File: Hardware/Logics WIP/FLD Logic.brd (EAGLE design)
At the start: 60.6 x 33 mm, 82 parts

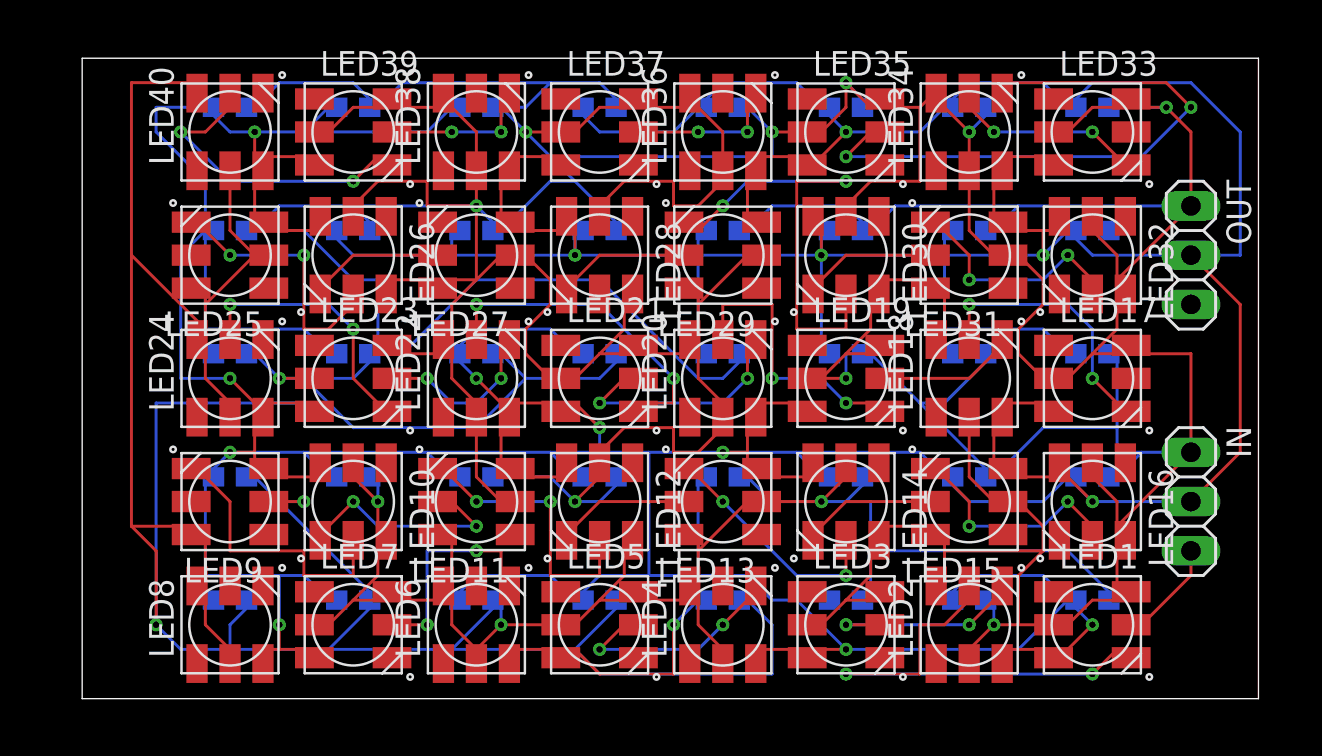
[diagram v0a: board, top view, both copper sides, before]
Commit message: 
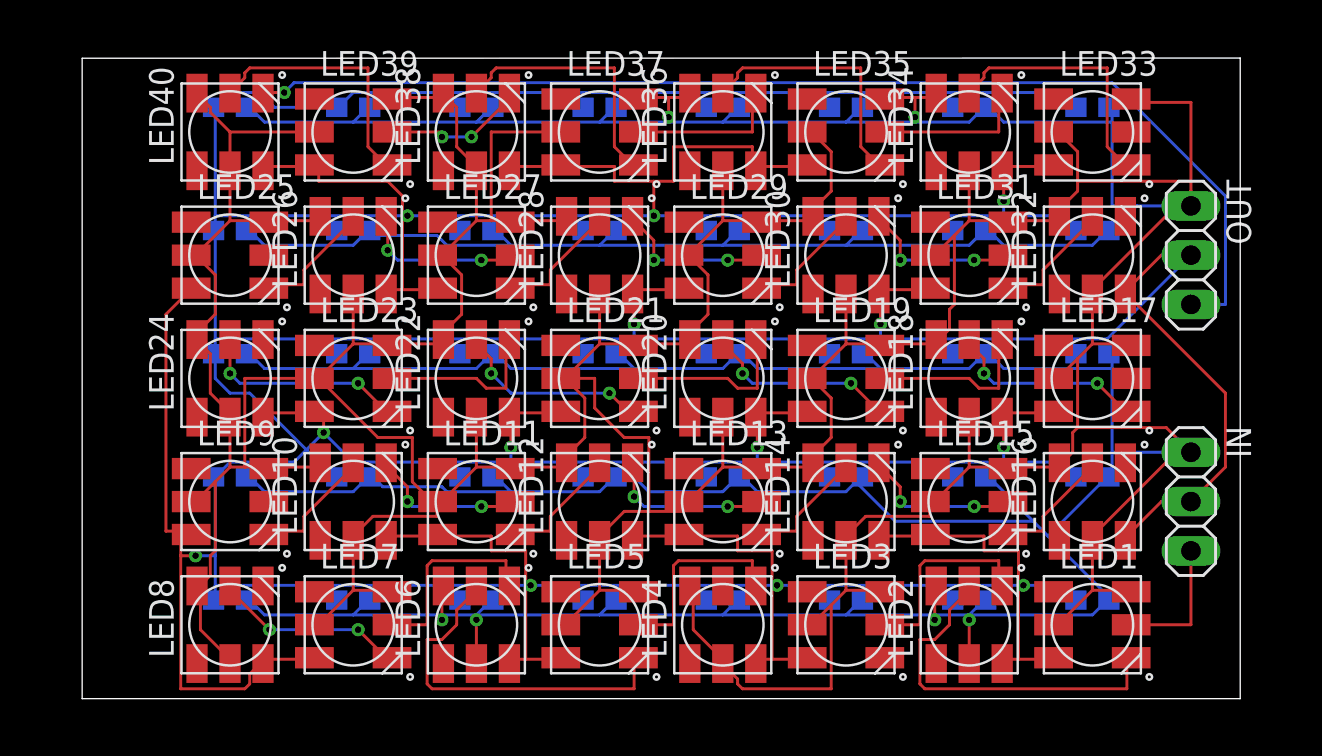
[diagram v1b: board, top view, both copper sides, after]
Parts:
- turned LED10 to 90 degrees
- turned LED11 to 0 degrees
- turned LED12 to 90 degrees
- turned LED13 to 0 degrees
- turned LED14 to 90 degrees
- turned LED15 to 0 degrees
- turned LED16 to 90 degrees
- turned LED25 to 0 degrees
- turned LED26 to 90 degrees
- turned LED27 to 0 degrees
- turned LED28 to 90 degrees
- turned LED29 to 0 degrees
- turned LED30 to 90 degrees
- turned LED31 to 0 degrees
- turned LED32 to 90 degrees
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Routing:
- net +5V: track 746.6 -> 637.9 mm, vias 15 -> 6
- net DOUT: track 0.00 -> 59.6 mm, vias 0 -> 1
- net N$33: track 32.7 -> 7.94 mm, vias 2 -> 0
- net N$2: track 0.00 -> 19.1 mm
- net GND: track 496.5 -> 478.6 mm, vias 15 -> 13
- net N$27: track 24.0 -> 6.53 mm, vias 2 -> 0
- net N$35: track 0.00 -> 13.6 mm
- net N$36: track 0.00 -> 13.6 mm
- net N$4: track 0.00 -> 10.1 mm, vias 0 -> 2
- net N$13: track 14.6 -> 6.53 mm, vias 2 -> 0
- net N$7: track 14.6 -> 6.53 mm
- net N$24: track 13.9 -> 6.53 mm, vias 2 -> 0
- net N$28: track 0.00 -> 6.53 mm
- net N$11: track 25.5 -> 19.1 mm, vias 2 -> 0
- net N$19: track 16.8 -> 10.4 mm
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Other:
- board size 60.6 x 33 mm -> 59.7 x 33 mm

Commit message: 
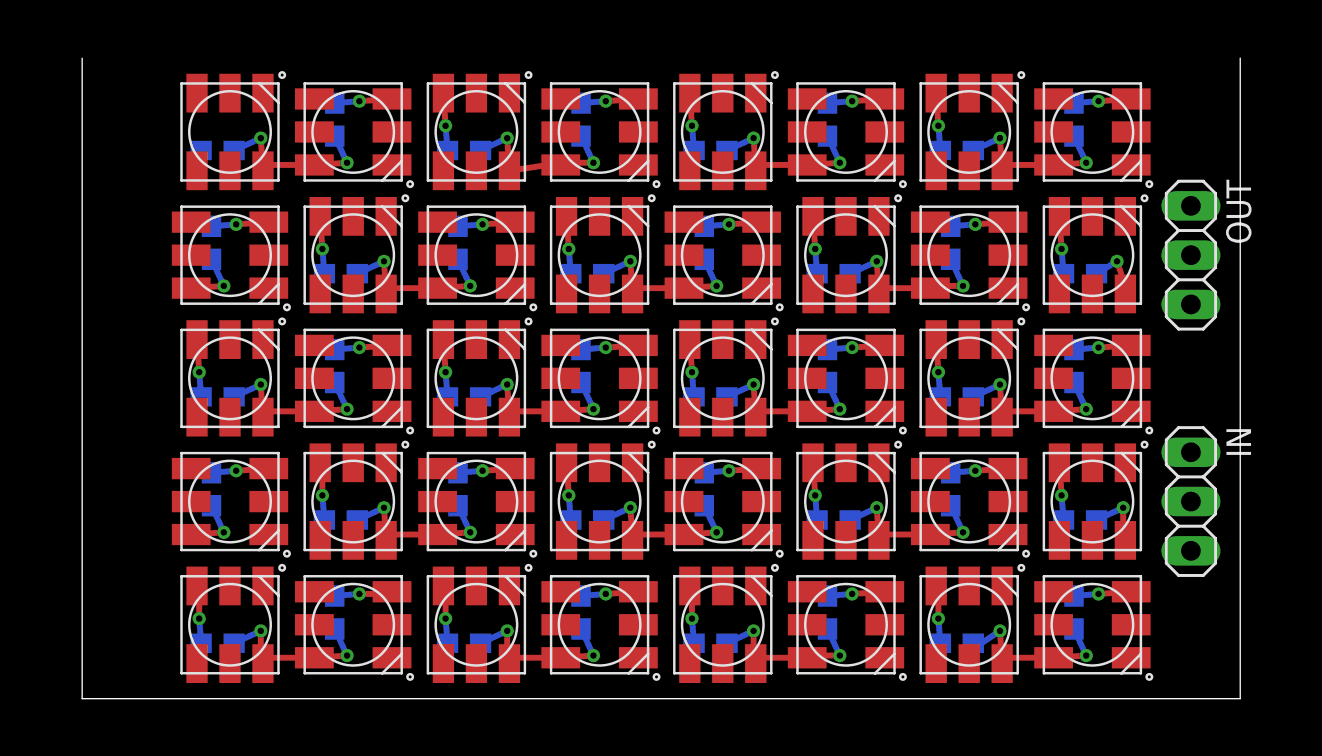
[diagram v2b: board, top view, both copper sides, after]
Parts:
- moved C20 2.31 mm to (32.4, 15.6), turned to 180 degrees
- moved C22 2.31 mm to (19.7, 15.6), turned to 180 degrees
- moved C24 2.31 mm to (6.99, 15.6), turned to 180 degrees
- moved C18 2.31 mm to (45.1, 15.6), turned to 180 degrees
- moved C36 2.31 mm to (32.4, 28.3), turned to 180 degrees
- moved C4 2.31 mm to (32.4, 2.86)
- moved C12 2.31 mm to (26.0, 9.21), turned to 180 degrees
- moved C28 2.31 mm to (26.0, 21.9), turned to 180 degrees
- moved C38 2.31 mm to (19.7, 28.3), turned to 180 degrees
- moved C6 2.31 mm to (19.7, 2.86), turned to 180 degrees
- moved C10 2.31 mm to (13.3, 9.21), turned to 180 degrees
- moved C26 2.31 mm to (13.3, 21.9), turned to 180 degrees
- moved C40 2.31 mm to (6.99, 28.3), turned to 180 degrees
- moved C8 2.31 mm to (6.99, 2.86), turned to 180 degrees
- moved C14 2.31 mm to (38.7, 9.21), turned to 180 degrees
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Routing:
- net +5V: track 637.9 -> 109.1 mm, vias 6 -> 38
- net GND: track 478.6 -> 174.8 mm, vias 13 -> 41
- net DOUT: track 59.6 -> 0.00 mm, vias 1 -> 0
- net N$2: track 19.1 -> 0.00 mm
- net N$11: track 19.1 -> 0.00 mm
- net N$37: track 13.6 -> 0.00 mm
- net N$35: track 13.6 -> 0.00 mm
- net N$32: track 13.6 -> 0.00 mm
- net N$36: track 13.6 -> 0.00 mm
- net N$21: track 11.0 -> 0.00 mm, vias 2 -> 0
- net N$6: track 10.5 -> 0.00 mm, vias 2 -> 0
- net N$12: track 10.5 -> 0.00 mm
- net N$5: track 10.5 -> 0.00 mm
- net N$1: track 10.5 -> 0.00 mm
- net N$19: track 10.4 -> 0.00 mm, vias 2 -> 0
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
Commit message: 
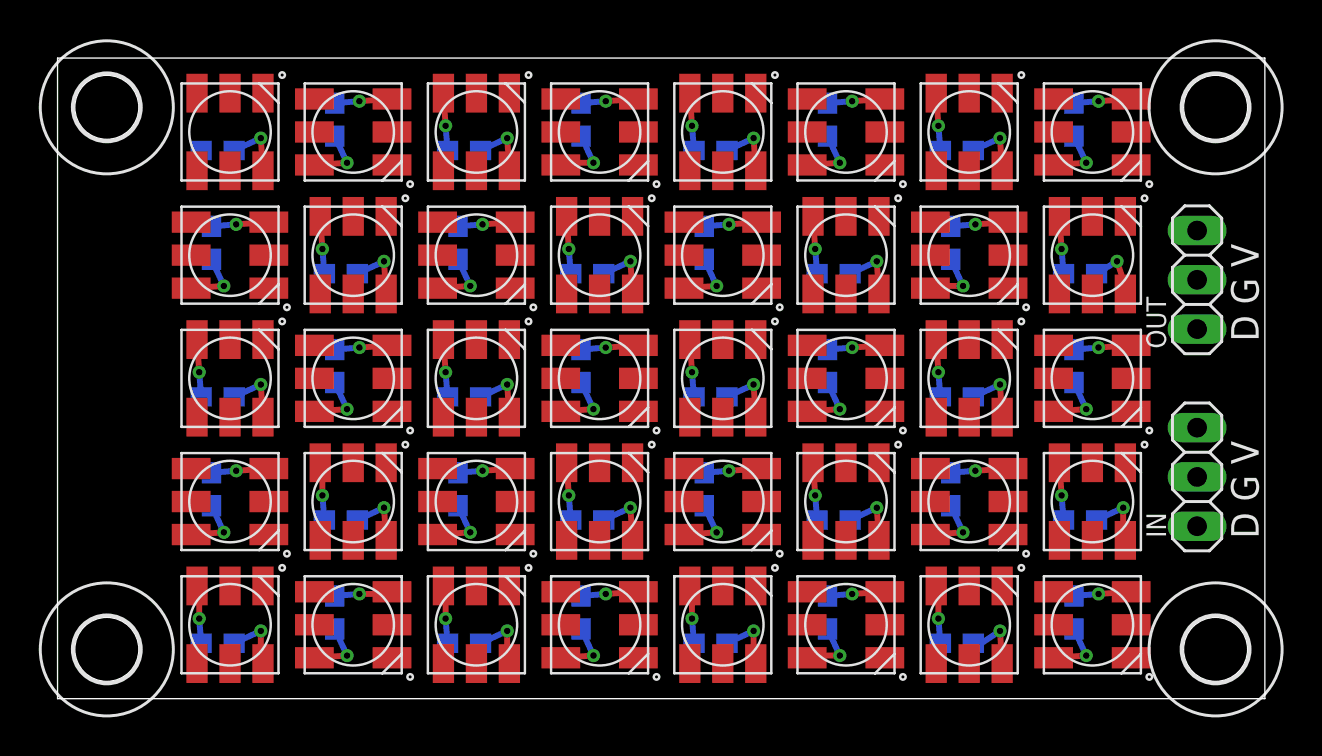
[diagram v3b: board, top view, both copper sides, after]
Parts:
- added H1, H2, H3, H4: MOUNT-HOLE3.3, holes:3,3
- moved IN 1.31 mm to (57.5, 11.4)
- moved OUT 1.31 mm to (57.5, 21.6)
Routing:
- net GND: track 174.8 -> 128.2 mm
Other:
- board size 59.7 x 33 mm -> 62.2 x 33 mm
- board text added: "D G V"

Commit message: 
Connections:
- net +5V: now also IN.2, OUT.2; no longer IN.1, OUT.1
- net GND: now also IN.1, OUT.1; no longer IN.2, OUT.2
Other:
- board text added: "D + G"
- board text removed: "D G V"
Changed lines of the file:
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@@
 <setting verticaltext="up"/>
 </settings>
-<grid distance="0.0125" unitdist="inch" unit="inch" style="lines" multiple="1" display="yes" altdistance="0.025" altunitdist="inch" altunit="inch"/>
+<grid distance="0.05" unitdist="inch" unit="inch" style="lines" multiple="1" display="yes" altdistance="0.025" altunitdist="inch" altunit="inch"/>
 <layers>
 <layer number="1" name="Top" color="4" fill="1" visible="yes" active="yes"/>
@@
 <wire x1="-1.27" y1="33.01" x2="-1.27" y2="0" width="0" layer="20"/>
 <wire x1="-1.27" y1="33.02" x2="60.96" y2="33.02" width="0" layer="20"/>
-<text x="60.6425" y="8.255" size="1.4224" layer="21" font="vector" rot="R90">D G V</text>
-<text x="60.6425" y="18.415" size="1.4224" layer="21" font="vector" rot="R90">D G V</text>
+<text x="60.6425" y="8.255" size="1.4224" layer="21" font="vector" rot="R90">D + G</text>
+<text x="60.6425" y="18.415" size="1.4224" layer="21" font="vector" rot="R90">D + G</text>
 </plain>
 <attributes>
@@
 <element name="C40" library="adafruit" package="C0603" value="0.1uF" x="6.985" y="28.2575" smashed="yes" rot="MR180"/>
 <element name="OUT" library="pinhead" package="1X03" value="" x="57.4675" y="21.59" smashed="yes" rot="R270">
-<attribute name="NAME" x="54.8513" y="20.7137" size="1.016" layer="25" font="vector" ratio="10" rot="R270"/>
+<attribute name="NAME" x="54.8513" y="21.9837" size="1.016" layer="25" font="vector" ratio="10" rot="R270"/>
 <attribute name="VALUE" x="54.2925" y="25.4" size="1.27" layer="27" rot="R270"/>
 </element>
@@
 <contactref element="C2" pad="2"/>
 <contactref element="C3" pad="2"/>
-<contactref element="IN" pad="2"/>
 <contactref element="LED1" pad="VSS"/>
 <contactref element="LED2" pad="VSS"/>
@@
 <contactref element="LED39" pad="VSS"/>
 <contactref element="LED40" pad="VSS"/>
-<contactref element="OUT" pad="2"/>
 <wire x1="7.835" y1="2.8575" x2="9.2075" y2="3.4925" width="0.3048" layer="16"/>
 <via x="9.2075" y="3.4925" extent="1-16" drill="0.3302" diameter="0.254" shape="octagon"/>
@@
 <wire x1="24.13" y1="27.5275" x2="24.13" y2="27.305" width="0.3048" layer="1"/>
 <wire x1="9.32" y1="27.51" x2="9.32" y2="27.21" width="0.3048" layer="1"/>
-<wire x1="53.77" y1="20.86" x2="57.4675" y2="21.59" width="0" layer="19" extent="1-1"/>
-<wire x1="53.6575" y1="21.59" x2="53.77" y2="20.86" width="0" layer="19" extent="1-1"/>
+<contactref element="IN" pad="1"/>
+<contactref element="OUT" pad="1"/>
+<wire x1="53.34" y1="22.5425" x2="57.4675" y2="24.13" width="0" layer="19" extent="1-1"/>
+<wire x1="53.77" y1="20.86" x2="53.6575" y2="21.59" width="0" layer="19" extent="1-1"/>
 <wire x1="51.1175" y1="16.295" x2="53.77" y2="20.86" width="0" layer="19" extent="1-16"/>
 <wire x1="47.42" y1="14.81" x2="50.07" y2="14.81" width="0" layer="19" extent="1-1"/>
@@
 <wire x1="53.77" y1="8.16" x2="51.1175" y2="3.595" width="0" layer="19" extent="1-16"/>
 <wire x1="53.6575" y1="8.89" x2="53.77" y2="8.16" width="0" layer="19" extent="1-1"/>
-<wire x1="57.4675" y1="11.43" x2="53.6575" y2="9.8425" width="0" layer="19" extent="1-1"/>
 <wire x1="34.72" y1="14.51" x2="32.0675" y2="9.945" width="0" layer="19" extent="1-16"/>
 <wire x1="37.37" y1="14.81" x2="34.72" y2="14.81" width="0" layer="19" extent="1-1"/>
@@
 <wire x1="9.32" y1="27.51" x2="11.97" y2="27.51" width="0" layer="19" extent="1-1"/>
 <wire x1="6.6675" y1="22.645" x2="9.32" y2="27.21" width="0" layer="19" extent="1-16"/>
+<wire x1="57.4675" y1="13.97" x2="53.6575" y2="9.8425" width="0" layer="19" extent="1-1"/>
 </signal>
 <signal name="+5V">
@@
 <contactref element="LED3" pad="LEDVDD"/>
 <contactref element="LED3" pad="VDD"/>
-<contactref element="IN" pad="1"/>
 <contactref element="C4" pad="1"/>
 <contactref element="LED4" pad="VDD"/>
@@
 <contactref element="LED40" pad="LEDVDD"/>
 <contactref element="LED40" pad="VDD"/>
-<contactref element="OUT" pad="1"/>
 <wire x1="6.135" y1="2.8575" x2="6.0325" y2="4.1275" width="0.3048" layer="16"/>
 <via x="6.0325" y="4.1275" extent="1-16" drill="0.3302" diameter="0.254" shape="octagon"/>
@@
 <via x="52.3875" y="30.7975" extent="1-16" drill="0.3302" diameter="0.254" shape="octagon"/>
 <wire x1="52.3875" y1="30.7975" x2="51.1175" y2="30.695" width="0.3048" layer="16"/>
-<wire x1="52.07" y1="20.86" x2="57.4675" y2="24.13" width="0" layer="19" extent="1-1"/>
-<wire x1="50.585" y1="21.9075" x2="52.07" y2="20.86" width="0" layer="19" extent="1-16"/>
+<contactref element="IN" pad="2"/>
+<contactref element="OUT" pad="2"/>
+<wire x1="50.07" y1="29.21" x2="51.1175" y2="30.695" width="0" layer="19" extent="1-16"/>
+<wire x1="50.37" y1="24.86" x2="50.07" y2="29.21" width="0" layer="19" extent="1-1"/>
+<wire x1="52.07" y1="20.86" x2="50.585" y2="21.9075" width="0" layer="19" extent="1-16"/>
 <wire x1="47.72" y1="24.56" x2="50.37" y2="24.86" width="0" layer="19" extent="1-1"/>
 <wire x1="43.72" y1="22.86" x2="44.7675" y2="24.345" width="0" layer="19" extent="1-16"/>
@@
 <wire x1="52.3875" y1="18.0975" x2="52.07" y2="20.86" width="0" layer="19" extent="1-1"/>
 <wire x1="50.07" y1="16.51" x2="51.1175" y2="17.995" width="0" layer="19" extent="1-16"/>
-<wire x1="50.07" y1="29.21" x2="50.37" y2="24.86" width="0" layer="19" extent="1-1"/>
-<wire x1="51.1175" y1="30.695" x2="50.07" y2="29.21" width="0" layer="19" extent="1-16"/>
 <wire x1="44.02" y1="18.51" x2="43.72" y2="22.86" width="0" layer="19" extent="1-1"/>
 <wire x1="45.72" y1="14.51" x2="44.235" y2="15.5575" width="0" layer="19" extent="1-16"/>
@@
 <wire x1="6.0325" y1="5.08" x2="5.92" y2="5.81" width="0" layer="19" extent="1-1"/>
 <wire x1="7.62" y1="1.81" x2="6.135" y2="2.8575" width="0" layer="19" extent="1-16"/>
-<wire x1="57.4675" y1="13.97" x2="54.07" y2="18.21" width="0" layer="19" extent="1-1"/>
+<wire x1="57.4675" y1="21.59" x2="54.07" y2="18.21" width="0" layer="19" extent="1-1"/>
+<wire x1="57.4675" y1="11.43" x2="52.07" y2="8.16" width="0" layer="19" extent="1-1"/>
 </signal>
 <signal name="N$11">

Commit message: 
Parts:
- moved OUT 55.5 mm to (2.22, 16.5), flipped to the bottom
- moved IN 5.08 mm to (57.5, 16.5)
- moved H1 0.64 mm to (1.91, 2.54)
- moved H3 0.64 mm to (1.91, 30.5)
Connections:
- net N$16: now also LED17.DI
- net N$41: now also LED9.DI
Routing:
- net +5V: track 109.1 -> 112.1 mm, vias 38 -> 39
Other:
- board text removed: "D + G"

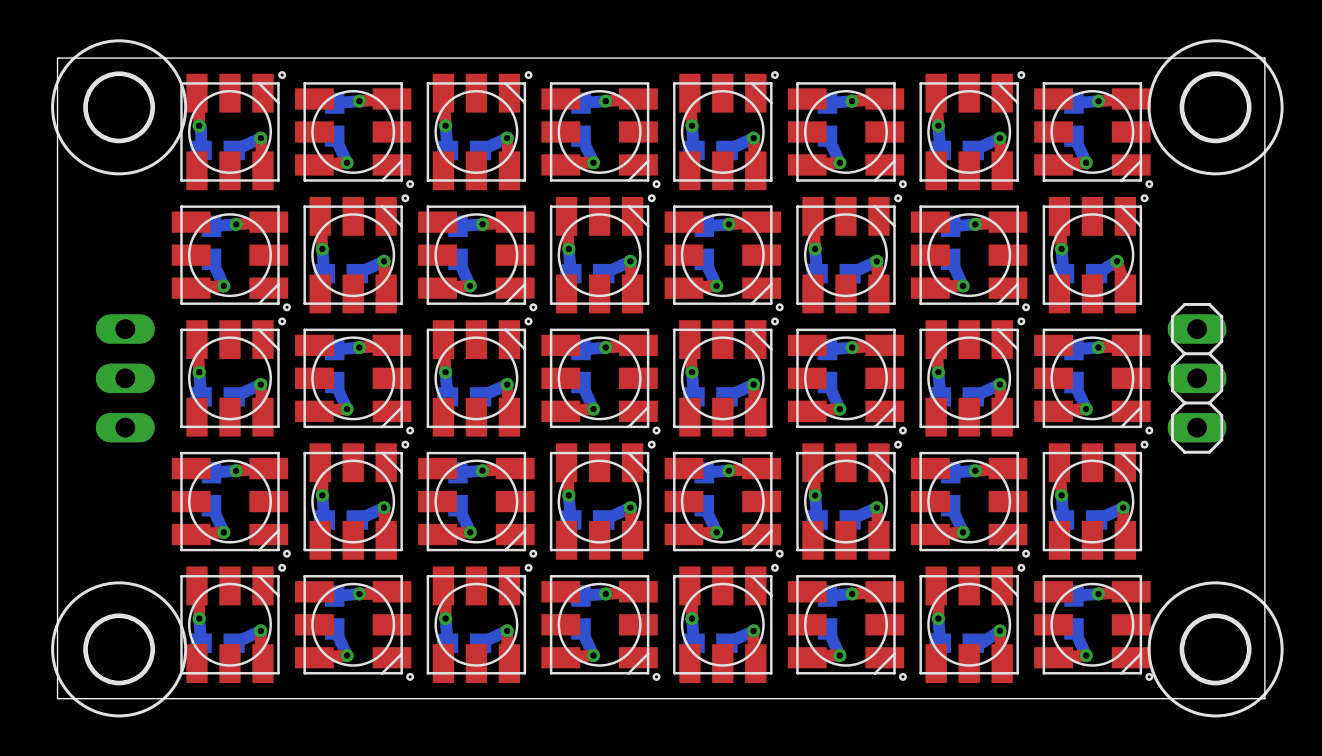
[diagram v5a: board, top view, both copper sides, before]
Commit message: 
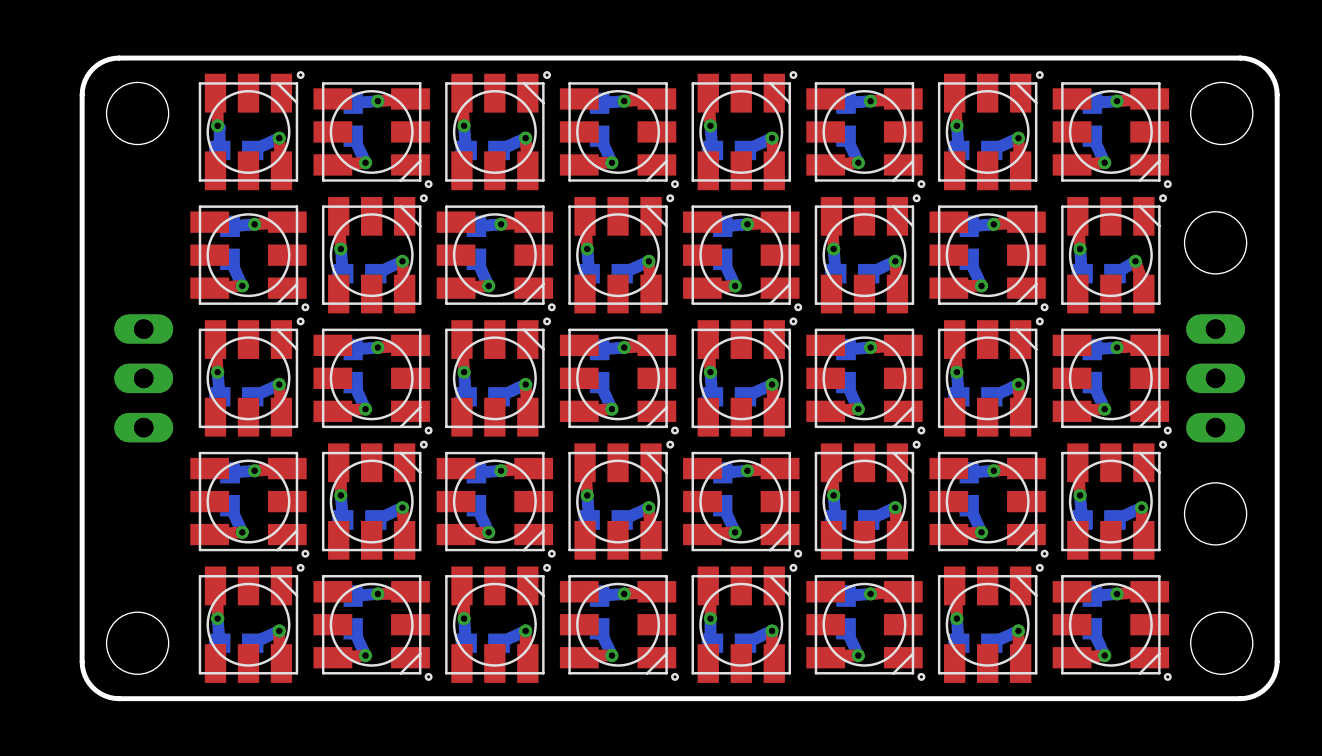
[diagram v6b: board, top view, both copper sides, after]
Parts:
- removed H1, H2, H3, H4: MOUNT-HOLE3.3, holes:3,3
- moved C1 0.95 mm to (52.1, 4.45)
- moved C11 0.95 mm to (20.3, 10.8)
- moved C12 0.95 mm to (27.0, 9.21)
- moved C13 0.95 mm to (33.0, 10.8)
- moved C14 0.95 mm to (39.7, 9.21)
- moved C15 0.95 mm to (45.7, 10.8)
- moved C16 0.95 mm to (52.4, 9.21)
- moved C17 0.95 mm to (52.1, 17.1)
- moved C18 0.95 mm to (46.0, 15.6)
- moved C19 0.95 mm to (39.4, 17.1)
- moved C2 0.95 mm to (46.0, 2.86), turned to 180 degrees
- moved C20 0.95 mm to (33.3, 15.6)
- moved C21 0.95 mm to (26.7, 17.1)
- moved C22 0.95 mm to (20.6, 15.6)
- moved C23 0.95 mm to (14.0, 17.1)
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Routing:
- net GND: track 128.2 -> 125.5 mm, vias 41 -> 40
- net +5V: track 112.1 -> 114.2 mm, vias 39 -> 40
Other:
- board size 62.2 x 33 mm -> 61.6 x 33 mm
- board text added: "+ -"
